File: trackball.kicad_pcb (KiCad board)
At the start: 2 copper layers, 27.5 x 35.2 mm, 37 parts, among them P1 CONN_10, P2 CONN_5, U1 MKL03Z32VFK4, U2 ADNS-3530, U4 ESD

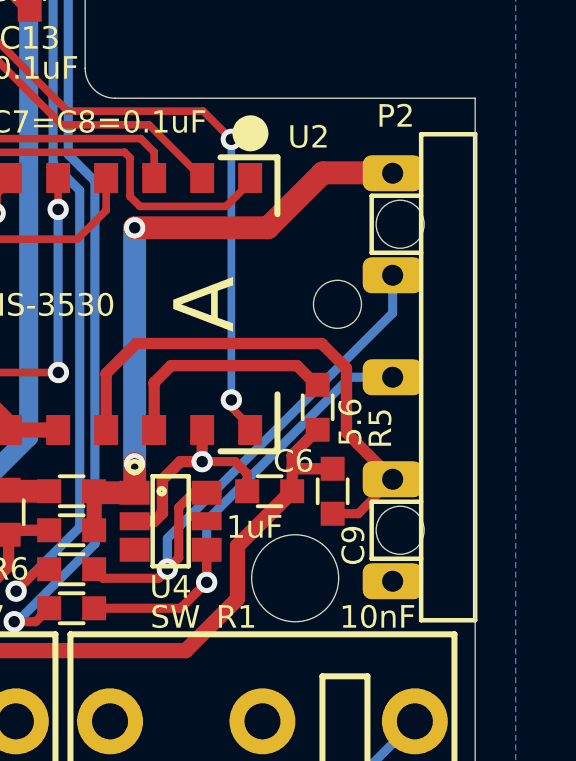
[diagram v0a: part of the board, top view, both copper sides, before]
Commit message: Display part number for the pogo pin connector.
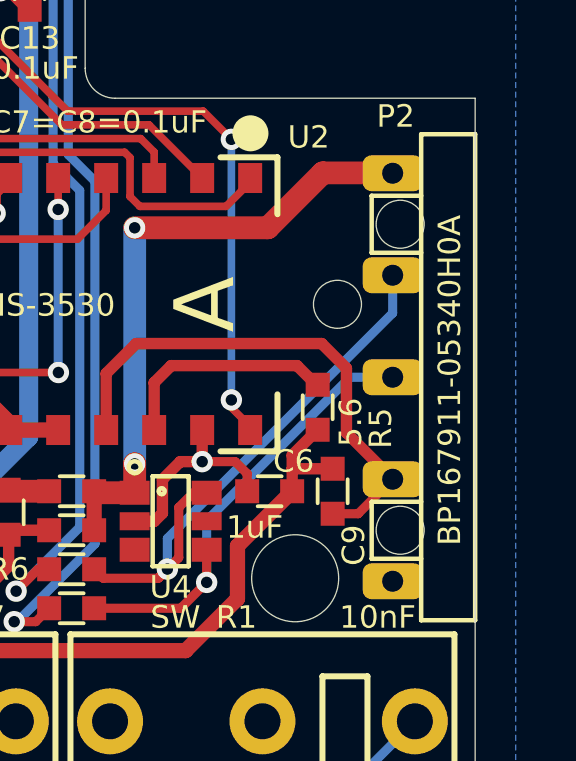
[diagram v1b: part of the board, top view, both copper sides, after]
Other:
- board text added: "BP167911-05340H0A"
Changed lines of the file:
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@@
   (general
     (thickness 1.6)
-    (drawings 42)
+    (drawings 43)
     (tracks 366)
     (zones 0)
@@
       (clearance 0.00001))
   )
+  (gr_text BP167911-05340H0A (at 208.8 133.1 90) (layer F.SilkS)
+    (effects (font (size 0.75 0.75) (thickness 0.15)))
+  )
   (gr_text C7=C8=0.1uF (at 197.1 124.5) (layer F.SilkS)

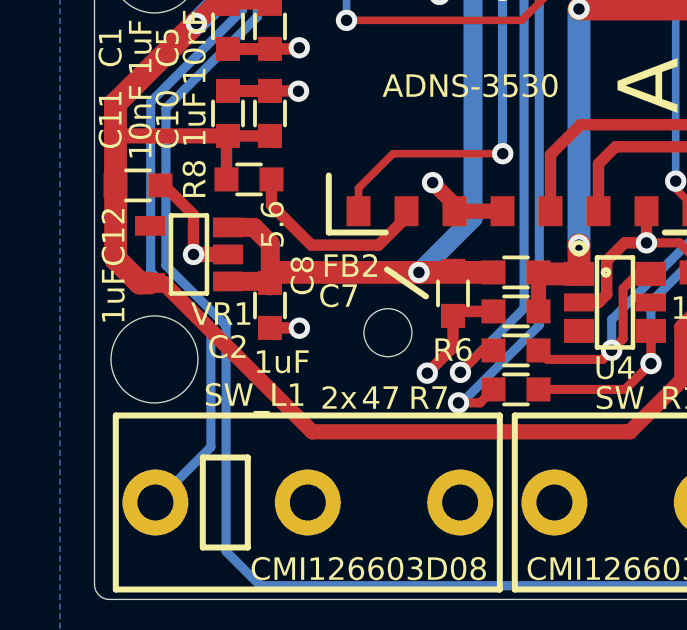
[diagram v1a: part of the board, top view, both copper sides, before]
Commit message: Add UHK logo.
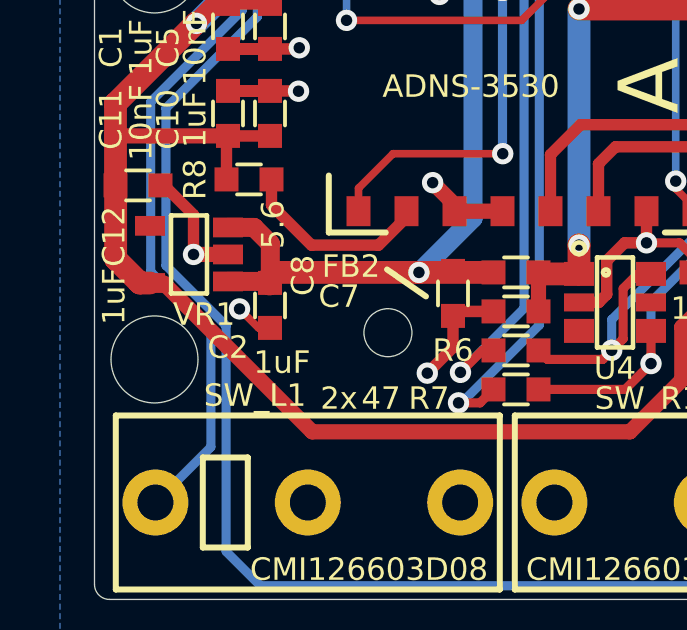
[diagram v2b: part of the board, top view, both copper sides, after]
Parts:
- added G***: LOGO, ugl:UHK_Logo_12x3.4_mm, B.Cu at (189.1, 135.7)

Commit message: Bump version number to 1.1.0
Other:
- board text added: "PCB ID: trackball_main_1.1.0"
- board text removed: "PCB ID: trackball_main_1.0.0"
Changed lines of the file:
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@@
   (title_block
     (title "UHK Trackball Module")
-    (rev 1.0.0)
+    (rev 1.1.0)
     (company "Ultimate Gadget Laboratories Kft.")
   )
@@
     (effects (font (size 0.738 0.738) (thickness 0.15148)))
   )
-  (gr_text "PCB ID: trackball_main_1.0.0" (at 195.9 146.8) (layer B.SilkS)
+  (gr_text "PCB ID: trackball_main_1.1.0" (at 195.9 146.8) (layer B.SilkS)
     (effects (font (size 0.75 0.75) (thickness 0.15)) (justify mirror))
   )

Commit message: Add UPA14 text.
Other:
- board text added: "UPA14"
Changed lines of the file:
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@@
   (general
     (thickness 1.6)
-    (drawings 43)
+    (drawings 44)
     (tracks 366)
     (zones 0)
@@
     (tags "Tag-Connect TC2050")
     (attr virtual)
-    (fp_text reference P1 (at 1.4044 2.5084) (layer F.SilkS)
+    (fp_text reference P1 (at -1.7 2.5) (layer F.SilkS)
       (effects (font (size 0.75 0.75) (thickness 0.15)))
     )
@@
       (clearance 0.00001))
   )
+  (gr_text UPA14 (at 200.7 118) (layer F.SilkS)
+    (effects (font (size 0.75 0.75) (thickness 0.15)))
+  )
   (gr_text BP167911-05340H0A (at 208.8 133.1 90) (layer F.SilkS)

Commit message: Rename UPA14 to UPA10.
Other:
- board text added: "UPA10"
- board text removed: "UPA14"
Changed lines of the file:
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@@
-(kicad_pcb (version 20171130) (host pcbnew 5.1.3-ffb9f22~84~ubuntu18.04.1)
+(kicad_pcb (version 20171130) (host pcbnew 5.1.4-e60b266~84~ubuntu18.04.1)
   (general
     (thickness 1.6)
@@
       (clearance 0.00001))
   )
-  (gr_text UPA14 (at 200.7 118) (layer F.SilkS)
+  (gr_text UPA10 (at 200.7 118) (layer F.SilkS)
     (effects (font (size 0.75 0.75) (thickness 0.15)))
   )

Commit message: Add clearances around mechanical holes.
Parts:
- removed the ? at (205.1, 130.6)
- removed the ? at (184.2, 139.7)
- removed the ? at (191.9, 138.8)
- removed the ? at (191.9, 122.3)
- removed the ? at (184.2, 126.7)
- removed the ? at (203.7, 139.7)
- added ?: , ugl:hole_2.9mm, F.Cu at (203.7, 139.7)
- added ?: , ugl:hole_2.9mm, F.Cu at (184.2, 139.7)
- added ?: , ugl:hole_2.9mm, F.Cu at (184.2, 126.7)
- added ?: , ugl:hole_1.6mm, B.Cu at (191.9, 138.8)
- added ?: , ugl:hole_1.6mm, B.Cu at (205.1, 130.6)
- added ?: , ugl:hole_1.6mm, B.Cu at (191.9, 122.3)

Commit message: Make pogo pin through hole, make logo virtual, make ESD text visible.
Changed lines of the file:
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@@
     (pad_to_mask_clearance 0)
     (aux_axis_origin 0 0)
-    (visible_elements 7FFFEF7F)
+    (visible_elements 7FFFEFFF)
     (pcbplotparams
       (layerselection 0x00030_ffffffff)
@@
   (module ugl:UHK_Logo_12x3.4_mm (layer B.Cu)
     (at 189.1 135.7 270)
+    (attr virtual)
     (fp_text reference G*** (at 0 0 270) (layer B.SilkS) hide
       (effects (font (size 1.524 1.524) (thickness 0.3)) (justify mirror))
@@
       (effects (font (size 0.75 0.75) (thickness 0.15)))
     )
-    (fp_text value ESD (at -2.1 0) (layer F.Fab) hide
+    (fp_text value ESD (at 2.5 1.2 270) (layer F.SilkS)
       (effects (font (size 0.75 0.75) (thickness 0.15)))
     )
@@
   (module ugl:UHK_Male_Pogo_Pin_v2 locked (layer F.Cu)
     (at 209.65 133.000003)
-    (attr virtual)
     (fp_text reference P2 (at -2.65 -8.700003) (layer F.SilkS)
       (effects (font (size 0.75 0.75) (thickness 0.15)))
